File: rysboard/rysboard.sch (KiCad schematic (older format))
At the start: 8 parts, among them J1 RPi4, J17 Conn_01x03, J18 Conn_01x05, U4 STM32G030K8Tx

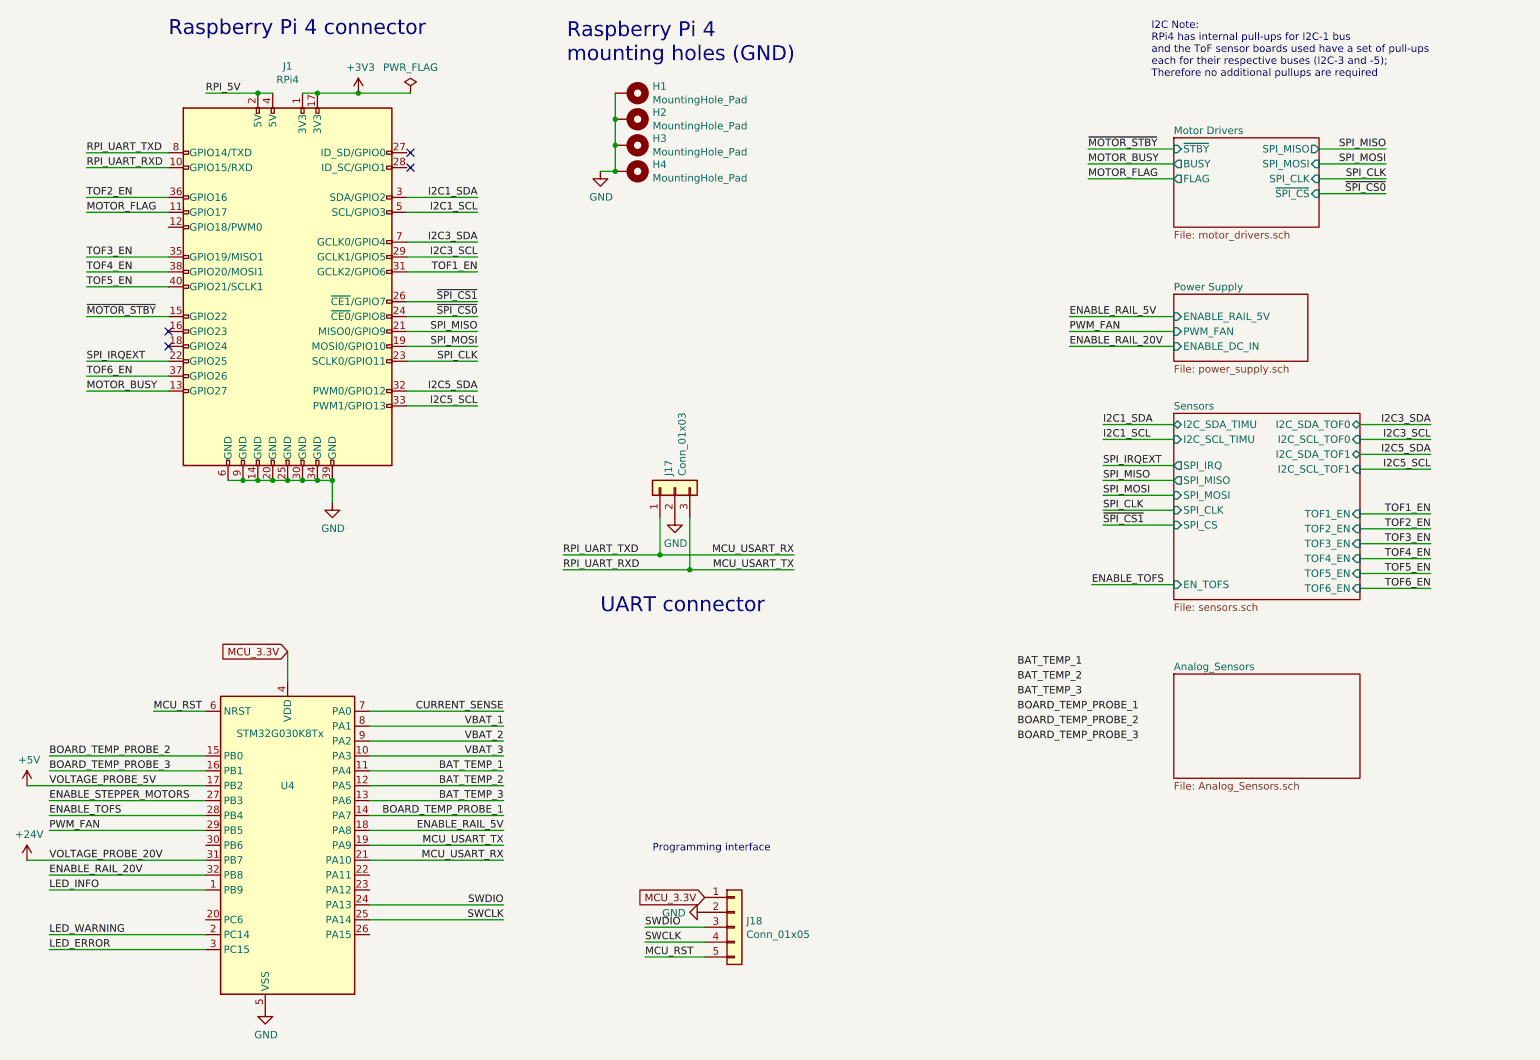
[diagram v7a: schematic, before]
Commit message: added some of the analog sensors
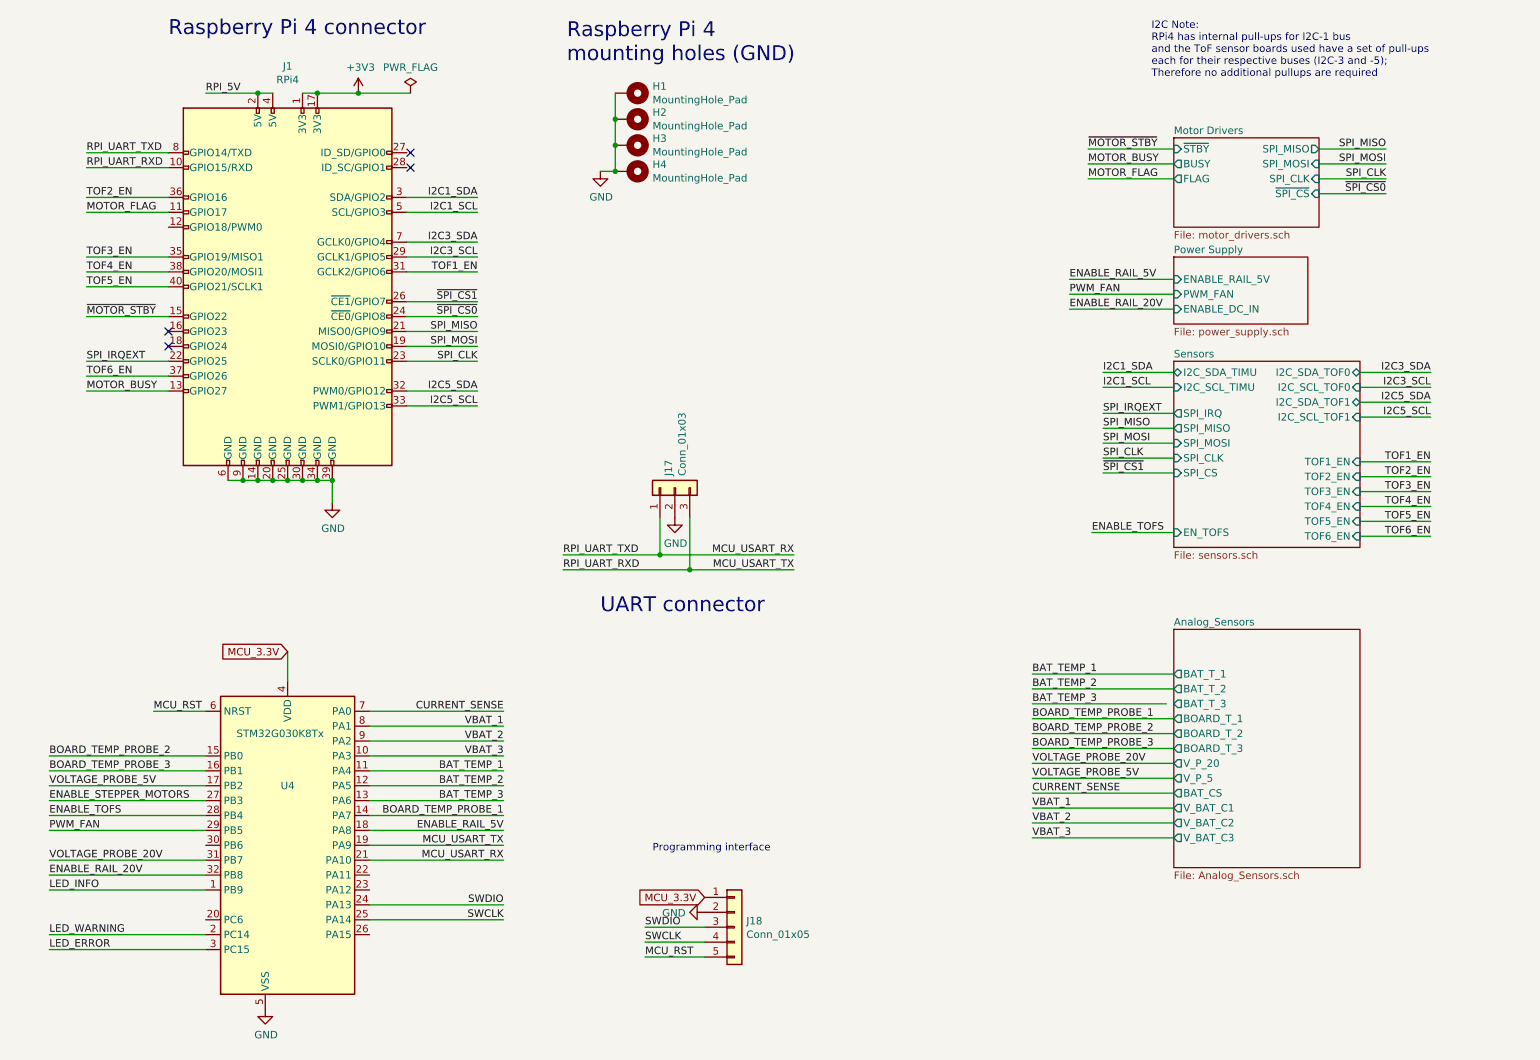
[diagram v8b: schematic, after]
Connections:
- net +24V renamed VOLTAGE_PROBE_20V
- net +5V renamed VOLTAGE_PROBE_5V
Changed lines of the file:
@@
 Raspberry Pi 4 connector
 $Sheet
-S 8250 2550 900  450
+S 8250 2300 900  450
 U 5E8FCBC6
 F0 "Power Supply" 50
 F1 "power_supply.sch" 50
-F2 "ENABLE_RAIL_5V" I L 8250 2700 50
-F3 "PWM_FAN" I L 8250 2800 50
-F4 "ENABLE_DC_IN" I L 8250 2900 50
+F2 "ENABLE_RAIL_5V" I L 8250 2450 50
+F3 "PWM_FAN" I L 8250 2550 50
+F4 "ENABLE_DC_IN" I L 8250 2650 50
 $EndSheet
 Text Label 3575 2700 2    50   ~ 0
@@
 Text Label 9675 1875 2    50   ~ 0
 ~SPI_CS0
-Text Label 7775 3800 0    50   ~ 0
+Text Label 7775 3450 0    50   ~ 0
 SPI_MISO
-Text Label 7775 3900 0    50   ~ 0
+Text Label 7775 3550 0    50   ~ 0
 SPI_MOSI
-Text Label 7775 4000 0    50   ~ 0
+Text Label 7775 3650 0    50   ~ 0
 SPI_CLK
-Text Label 7775 4100 0    50   ~ 0
+Text Label 7775 3750 0    50   ~ 0
 ~SPI_CS1
 Wire Wire Line
-	8250 3800 7775 3800
-Wire Wire Line
-	7775 3900 8250 3900
-Wire Wire Line
-	8250 4000 7775 4000
-Wire Wire Line
-	7775 4100 8250 4100
-Wire Wire Line
-	9500 4025 9975 4025
-Wire Wire Line
-	9500 4125 9975 4125
-Text Label 9975 4025 2    50   ~ 0
+	8250 3450 7775 3450
+Wire Wire Line
+	7775 3550 8250 3550
+Wire Wire Line
+	8250 3650 7775 3650
+Wire Wire Line
+	7775 3750 8250 3750
+Wire Wire Line
+	9500 3675 9975 3675
+Wire Wire Line
+	9500 3775 9975 3775
+Text Label 9975 3675 2    50   ~ 0
 TOF1_EN
-Text Label 9975 4125 2    50   ~ 0
+Text Label 9975 3775 2    50   ~ 0
 TOF2_EN
-Text Label 7775 3700 0    50   ~ 0
+Text Label 7775 3350 0    50   ~ 0
 SPI_IRQEXT
 Wire Wire Line
-	9500 4225 9975 4225
-Text Label 9975 4225 2    50   ~ 0
+	9500 3875 9975 3875
+Text Label 9975 3875 2    50   ~ 0
 TOF3_EN
-Text Label 9975 4325 2    50   ~ 0
+Text Label 9975 3975 2    50   ~ 0
 TOF4_EN
-Text Label 9975 4425 2    50   ~ 0
+Text Label 9975 4075 2    50   ~ 0
 TOF5_EN
-Text Label 9975 4525 2    50   ~ 0
+Text Label 9975 4175 2    50   ~ 0
 TOF6_EN
 Wire Wire Line
-	9500 4325 9975 4325
-Wire Wire Line
-	9500 4425 9975 4425
-Wire Wire Line
-	9500 4525 9975 4525
+	9500 3975 9975 3975
+Wire Wire Line
+	9500 4075 9975 4075
+Wire Wire Line
+	9500 4175 9975 4175
 NoConn ~ 3125 1700
 NoConn ~ 3125 1600
@@
 I2C5_SCL
 Wire Wire Line
-	7775 3700 8250 3700
+	7775 3350 8250 3350
 $Sheet
-S 8250 3350 1250 1250
+S 8250 3000 1250 1250
 U 5EA6D11C
 F0 "Sensors" 50
 F1 "sensors.sch" 50
-F2 "TOF6_EN" I R 9500 4525 50
-F3 "TOF5_EN" I R 9500 4425 50
-F4 "TOF4_EN" I R 9500 4325 50
-F5 "TOF2_EN" I R 9500 4125 50
-F6 "TOF1_EN" I R 9500 4025 50
-F7 "TOF3_EN" I R 9500 4225 50
-F8 "SPI_MOSI" I L 8250 3900 50
-F9 "SPI_MISO" O L 8250 3800 50
-F10 "SPI_CLK" I L 8250 4000 50
-F11 "SPI_CS" I L 8250 4100 50
-F12 "SPI_IRQ" O L 8250 3700 50
-F13 "I2C_SCL_TOF0" I R 9500 3525 50
-F14 "I2C_SDA_TOF0" B R 9500 3425 50
-F15 "I2C_SCL_TIMU" I L 8250 3525 50
-F16 "I2C_SDA_TIMU" B L 8250 3425 50
-F17 "I2C_SCL_TOF1" I R 9500 3725 50
-F18 "I2C_SDA_TOF1" B R 9500 3625 50
-F19 "EN_TOFS" I L 8250 4500 50
+F2 "TOF6_EN" I R 9500 4175 50
+F3 "TOF5_EN" I R 9500 4075 50
+F4 "TOF4_EN" I R 9500 3975 50
+F5 "TOF2_EN" I R 9500 3775 50
+F6 "TOF1_EN" I R 9500 3675 50
+F7 "TOF3_EN" I R 9500 3875 50
+F8 "SPI_MOSI" I L 8250 3550 50
+F9 "SPI_MISO" O L 8250 3450 50
+F10 "SPI_CLK" I L 8250 3650 50
+F11 "SPI_CS" I L 8250 3750 50
+F12 "SPI_IRQ" O L 8250 3350 50
+F13 "I2C_SCL_TOF0" I R 9500 3175 50
+F14 "I2C_SDA_TOF0" B R 9500 3075 50
+F15 "I2C_SCL_TIMU" I L 8250 3175 50
+F16 "I2C_SDA_TIMU" B L 8250 3075 50
+F17 "I2C_SCL_TOF1" I R 9500 3375 50
+F18 "I2C_SDA_TOF1" B R 9500 3275 50
+F19 "EN_TOFS" I L 8250 4150 50
 $EndSheet
 $Comp
@@
 RPI_UART_RXD
 Wire Wire Line
-	9500 3425 9975 3425
-Wire Wire Line
-	9500 3525 9975 3525
-Wire Wire Line
-	9500 3725 9975 3725
-Wire Wire Line
-	9500 3625 9975 3625
-Wire Wire Line
-	7775 3425 8250 3425
-Wire Wire Line
-	7775 3525 8250 3525
-Text Label 7775 3425 0    50   ~ 0
+	9500 3075 9975 3075
+Wire Wire Line
+	9500 3175 9975 3175
+Wire Wire Line
+	9500 3375 9975 3375
+Wire Wire Line
+	9500 3275 9975 3275
+Wire Wire Line
+	7775 3075 8250 3075
+Wire Wire Line
+	7775 3175 8250 3175
+Text Label 7775 3075 0    50   ~ 0
 I2C1_SDA
-Text Label 7775 3525 0    50   ~ 0
+Text Label 7775 3175 0    50   ~ 0
 I2C1_SCL
-Text Label 9975 3425 2    50   ~ 0
+Text Label 9975 3075 2    50   ~ 0
 I2C3_SDA
-Text Label 9975 3525 2    50   ~ 0
+Text Label 9975 3175 2    50   ~ 0
 I2C3_SCL
-Text Label 9975 3625 2    50   ~ 0
+Text Label 9975 3275 2    50   ~ 0
 I2C5_SDA
-Text Label 9975 3725 2    50   ~ 0
+Text Label 9975 3375 2    50   ~ 0
 I2C5_SCL
 Text Label 3575 2400 2    50   ~ 0
@@
 	4150 4400 5000 4400
 Connection ~ 5000 4400
-Text Label 7550 2700 0    50   ~ 0
+Text Label 7550 2450 0    50   ~ 0
 ENABLE_RAIL_5V
-Text Label 7550 2800 0    50   ~ 0
+Text Label 7550 2550 0    50   ~ 0
 PWM_FAN
-Text Label 7550 2900 0    50   ~ 0
+Text Label 7550 2650 0    50   ~ 0
 ENABLE_RAIL_20V
 Wire Wire Line
-	7550 2700 8250 2700
-Wire Wire Line
-	7550 2800 8250 2800
-Wire Wire Line
-	7550 2900 8250 2900
-$Comp
-L power:+24V #PWR?
-U 1 1 606D377E
-P 550 6350
-F 0 "#PWR?" H 550 6200 50  0001 C CNN
-F 1 "+24V" H 565 6523 50  0000 C CNN
-F 2 "" H 550 6350 50  0001 C CNN
-F 3 "" H 550 6350 50  0001 C CNN
-	1    550  6350
-	1    0    0    -1
-$EndComp
-Text Label 7700 4500 0    50   ~ 0
+	7550 2450 8250 2450
+Wire Wire Line
+	7550 2550 8250 2550
+Wire Wire Line
+	7550 2650 8250 2650
+Text Label 7700 4150 0    50   ~ 0
 ENABLE_TOFS
 Wire Wire Line
-	7700 4500 8250 4500
+	7700 4150 8250 4150
 $Sheet
-S 8250 5100 1250 700
+S 8250 4800 1250 1600
 U 60370950
 F0 "Analog_Sensors" 50
 F1 "Analog_Sensors.sch" 50
+F2 "BAT_T_1" O L 8250 5100 50
+F3 "BAT_T_2" O L 8250 5200 50
+F4 "BAT_T_3" O L 8250 5300 50
+F5 "BOARD_T_1" O L 8250 5400 50
+F6 "BOARD_T_2" O L 8250 5500 50
+F7 "BOARD_T_3" O L 8250 5600 50
+F8 "V_P_20" O L 8250 5700 50
+F9 "V_P_5" O L 8250 5800 50
+F10 "BAT_CS" O L 8250 5900 50
+F11 "V_BAT_C1" O L 8250 6000 50
+F12 "V_BAT_C2" O L 8250 6100 50
+F13 "V_BAT_C3" O L 8250 6200 50
 $EndSheet
-Text Label 7200 5450 0    50   ~ 0
+Text Label 7300 5500 0    50   ~ 0
 BOARD_TEMP_PROBE_2
-Text Label 7200 5550 0    50   ~ 0
+Text Label 7300 5600 0    50   ~ 0
 BOARD_TEMP_PROBE_3
-Text Label 7200 5350 0    50   ~ 0
+Text Label 7300 5400 0    50   ~ 0
 BOARD_TEMP_PROBE_1
-Text Label 7200 5250 0    50   ~ 0
+Text Label 7300 5300 0    50   ~ 0
 BAT_TEMP_3
-Text Label 7200 5150 0    50   ~ 0
+Text Label 7300 5200 0    50   ~ 0
 BAT_TEMP_2
-Text Label 7200 5050 0    50   ~ 0
+Text Label 7300 5100 0    50   ~ 0
 BAT_TEMP_1
-$Comp
-L power:+5V #PWR?
-U 1 1 603726EA
-P 550 5850
-F 0 "#PWR?" H 550 5700 50  0001 C CNN
-F 1 "+5V" H 565 6023 50  0000 C CNN
-F 2 "" H 550 5850 50  0001 C CNN
-F 3 "" H 550 5850 50  0001 C CNN
-	1    550  5850
-	1    0    0    -1
-$EndComp
-Wire Wire Line
-	550  5850 1750 5850
-Wire Wire Line
-	550  6350 1750 6350
 Text Notes 4750 6300 0    50   ~ 0
 Programming interface\n
+Text Label 7300 5700 0    50   ~ 0
+VOLTAGE_PROBE_20V
+Wire Wire Line
+	700  6350 1750 6350
+Wire Wire Line
+	700  5850 1750 5850
+Text Label 7300 5800 0    50   ~ 0
+VOLTAGE_PROBE_5V
+Text Label 7300 5900 0    50   ~ 0
+CURRENT_SENSE
+Text Label 7300 6000 0    50   ~ 0
+VBAT_1
+Text Label 7300 6100 0    50   ~ 0
+VBAT_2
+Text Label 7300 6200 0    50   ~ 0
+VBAT_3
+Wire Wire Line
+	7300 6200 8250 6200
+Wire Wire Line
+	8250 6100 7300 6100
+Wire Wire Line
+	7300 6000 8250 6000
+Wire Wire Line
+	8250 5900 7300 5900
+Wire Wire Line
+	7300 5800 8250 5800
+Wire Wire Line
+	8250 5700 7300 5700
+Wire Wire Line
+	7300 5600 8250 5600
+Wire Wire Line
+	8250 5500 7300 5500
+Wire Wire Line
+	7300 5400 8250 5400
+Wire Wire Line
+	8200 5300 7300 5300
+Wire Wire Line
+	7300 5200 8250 5200
+Wire Wire Line
+	8250 5100 7300 5100
 $EndSCHEMATC
